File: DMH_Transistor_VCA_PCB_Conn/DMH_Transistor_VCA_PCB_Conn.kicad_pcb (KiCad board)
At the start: 2 copper layers, 48 x 175 mm, 0 parts

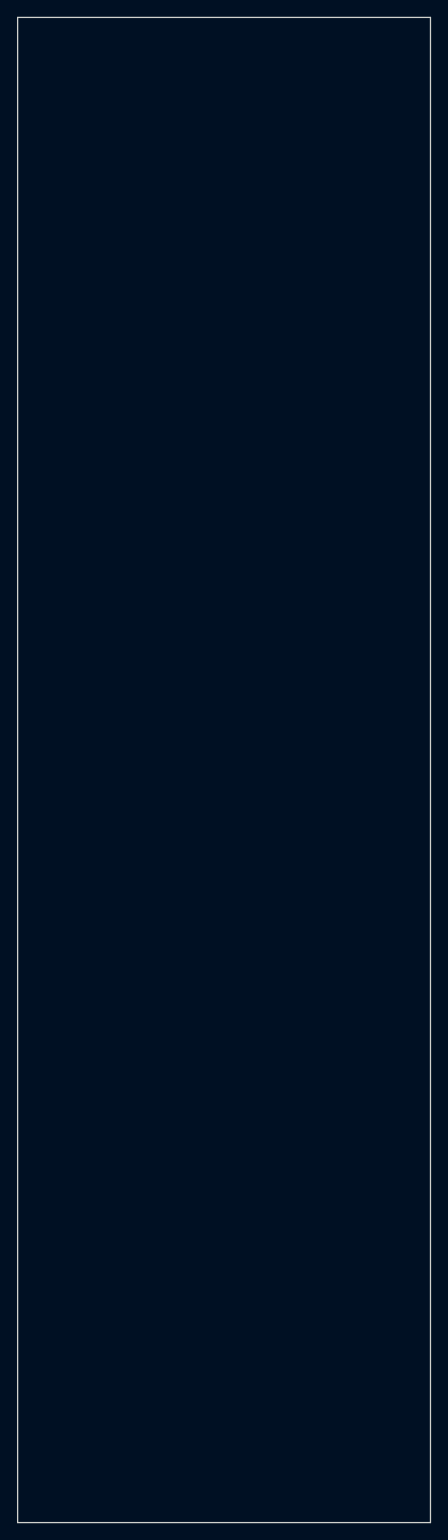
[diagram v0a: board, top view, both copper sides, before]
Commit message: Pots PCB in progress
Need to add CV input traces to the pin headers
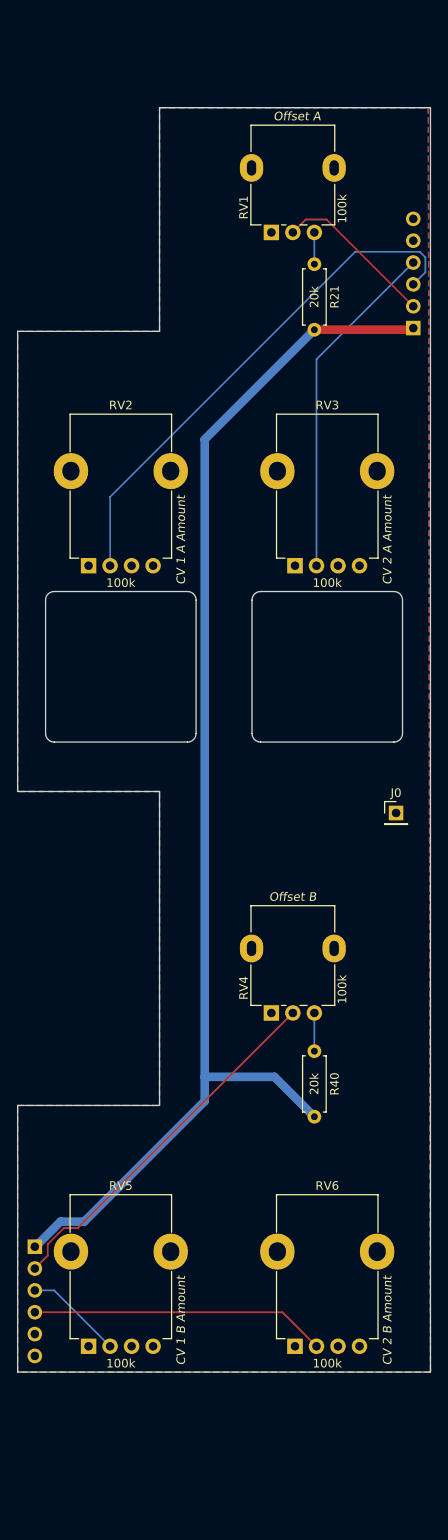
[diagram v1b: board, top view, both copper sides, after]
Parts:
- added J0: Conn_01x01, Connector_PinHeader_2.54mm:PinHeader_1x01_P2.54mm_Vertical, F.Cu at (95.0, 135.0)
- added J50: Conn_01x06, Connector_PinHeader_2.54mm:PinHeader_1x06_P2.54mm_Vertical, B.Cu at (97.0, 78.6)
- added J60: Conn_01x06, Connector_PinHeader_2.54mm:PinHeader_1x06_P2.54mm_Vertical, B.Cu at (53.0, 185.4)
- added R21: 20k, Resistor_THT:R_Axial_DIN0207_L6.3mm_D2.5mm_P7.62mm_Horizontal, F.Cu at (85.5, 71.2)
- added R40: 20k, Resistor_THT:R_Axial_DIN0207_L6.3mm_D2.5mm_P7.62mm_Horizontal, F.Cu at (85.5, 162.7)
- added RV1: 100k, SynthStuff:Potentiometer_Alpha_RD901F-40-00D_Single_Vertical, F.Cu at (80.5, 67.5)
- added RV2: 100k, SynthStuff:Potentiometer_TT_P110KH1, F.Cu at (60.5, 106.2)
- added RV3: 100k, SynthStuff:Potentiometer_TT_P110KH1, F.Cu at (84.5, 106.2)
- added RV4: 100k, SynthStuff:Potentiometer_Alpha_RD901F-40-00D_Single_Vertical, F.Cu at (80.5, 158.2)
- added RV5: 100k, SynthStuff:Potentiometer_TT_P110KH1, F.Cu at (60.5, 197.0)
- added RV6: 100k, SynthStuff:Potentiometer_TT_P110KH1, F.Cu at (84.5, 197.0)
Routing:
- net +12V: track 0.00 -> 148.0 mm
- net /Inputs and Outputs/CV 1 A Pot: track 0.00 -> 60.4 mm
- net /Inputs and Outputs/Offset B Pot: track 0.00 -> 43.1 mm
- net /Inputs and Outputs/CV 2 A Pot: track 0.00 -> 39.9 mm
- net /Inputs and Outputs/CV 2 B Pot: track 0.00 -> 34.4 mm
- net /Inputs and Outputs/Offset A Pot: track 0.00 -> 18.8 mm
- net /Inputs and Outputs/CV 1 B Pot: track 0.00 -> 11.4 mm
- net Net-(R40-Pad1): track 0.00 -> 4.44 mm
- net Net-(R21-Pad1): track 0.00 -> 3.69 mm
- added copper zone on B.Cu, net GND
- added copper zone on F.Cu, net GND
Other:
- board size 48 x 175 mm -> 48 x 147 mm

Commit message: Finished Pots PCB
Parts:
- J50, J60: value Conn_01x06 -> Conn_01x08; footprint Connector_PinHeader_2.54mm:PinHeader_1x06_P2.54mm_Vertical -> Connector_PinHeader_2.54mm:PinHeader_1x08_P2.54mm_Vertical
- moved J60 5.05 mm to (53.0, 180.4)
- moved J50 5.00 mm to (97.0, 83.6)
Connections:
- J50 pad 1: +12V -> /Inputs and Outputs/CV 1 A Jack
- J50 pad 2: /Inputs and Outputs/Offset A Pot -> /Inputs and Outputs/CV 2 A Jack
- J50 pad 3: /Inputs and Outputs/CV 1 A Pot -> +12V
- J50 pad 4: /Inputs and Outputs/CV 2 A Pot -> /Inputs and Outputs/Offset A Pot
- J50 pad 5: GND -> /Inputs and Outputs/CV 1 A Pot
- J50 pad 6: GND -> /Inputs and Outputs/CV 2 A Pot
- J60 pad 1: +12V -> /Inputs and Outputs/CV 1 B Jack
- J60 pad 2: /Inputs and Outputs/Offset B Pot -> /Inputs and Outputs/CV 2 B Jack
- J60 pad 3: /Inputs and Outputs/CV 1 B Pot -> +12V
- J60 pad 4: /Inputs and Outputs/CV 2 B Pot -> /Inputs and Outputs/Offset B Pot
- J60 pad 5: GND -> /Inputs and Outputs/CV 1 B Pot
- J60 pad 6: GND -> /Inputs and Outputs/CV 2 B Pot
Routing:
- net /Inputs and Outputs/CV 2 B Jack: track 0.00 -> 44.9 mm
- net /Inputs and Outputs/CV 1 A Jack: track 0.00 -> 42.1 mm
- net /Inputs and Outputs/CV 2 A Jack: track 0.00 -> 30.0 mm
- net /Inputs and Outputs/CV 1 B Jack: track 0.00 -> 27.8 mm

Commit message: Perfected pots (_conn) PCB
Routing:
- net /Inputs and Outputs/Offset B Pot: track 43.1 -> 45.4 mm
- net +12V: track 148.0 -> 146.8 mm
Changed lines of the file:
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@@
 			(pintype "passive")
 		)
-		(model "${KICAD8_3DMODEL_DIR}/Potentiometer_THT.3dshapes/Potentiometer_TT_P0915N.wrl"
+		(model "${KIPRJMOD}/Libraries/SynthStuff/3D_models/P110KH1_0F15BR10K.STEP"
 			(offset
-				(xyz 0 0 0)
+				(xyz 2.5 11 6)
 			)
 			(scale
@@
 			)
 			(rotate
-				(xyz 0 0 0)
+				(xyz 90 0 90)
 			)
 		)
@@
 			(pintype "passive")
 		)
-		(model "${KICAD8_3DMODEL_DIR}/Potentiometer_THT.3dshapes/Potentiometer_TT_P0915N.wrl"
+		(model "${KIPRJMOD}/Libraries/SynthStuff/3D_models/P110KH1_0F15BR10K.STEP"
 			(offset
-				(xyz 0 0 0)
+				(xyz 2.5 11 6)
 			)
 			(scale
@@
 			)
 			(rotate
-				(xyz 0 0 0)
+				(xyz 90 0 90)
 			)
 		)
 	)
 	(footprint "Connector_PinHeader_2.54mm:PinHeader_1x01_P2.54mm_Vertical"
-		(locked yes)
 		(layer "F.Cu")
 		(at 95 135)
@@
 		(sheetname "Inputs and Outputs")
 		(sheetfile "Inputs_and_Outputs.kicad_sch")
-		(attr through_hole)
+		(attr through_hole exclude_from_bom dnp)
 		(fp_line
 			(start -1.33 -1.33)
@@
 			(pintype "passive")
 		)
-		(model "${KICAD8_3DMODEL_DIR}/Potentiometer_THT.3dshapes/Potentiometer_TT_P0915N.wrl"
+		(model "${KIPRJMOD}/Libraries/SynthStuff/3D_models/P110KH1_0F15BR10K.STEP"
 			(offset
-				(xyz 0 0 0)
+				(xyz 2.5 11 6)
 			)
 			(scale
@@
 			)
 			(rotate
-				(xyz 0 0 0)
+				(xyz 90 0 90)
 			)
 		)
@@
 			(pintype "passive")
 		)
-		(model "${KICAD8_3DMODEL_DIR}/Potentiometer_THT.3dshapes/Potentiometer_TT_P0915N.wrl"
+		(model "${KIPRJMOD}/Libraries/SynthStuff/3D_models/P110KH1_0F15BR10K.STEP"
 			(offset
-				(xyz 0 0 0)
+				(xyz 2.5 11 6)
 			)
 			(scale
@@
 			)
 			(rotate
-				(xyz 0 0 0)
+				(xyz 90 0 90)
 			)
 		)
@@
 	)
 	(segment
-		(start 51.6 181.775)
-		(end 51.6 193.541346)
+		(start 61.5 194.25)
+		(end 64.25 197)
 		(width 0.2)
 		(layer "F.Cu")
@@
 	)
 	(segment
-		(start 51.6 193.541346)
-		(end 52.523654 194.465)
+		(start 52.308654 194.25)
+		(end 61.5 194.25)
 		(width 0.2)
 		(layer "F.Cu")
@@
 	)
 	(segment
-		(start 52.523654 194.465)
-		(end 61.715 194.465)
+		(start 51.6 181.775)
+		(end 51.6 193.541346)
 		(width 0.2)
 		(layer "F.Cu")
@@
 	)
 	(segment
-		(start 61.715 194.465)
-		(end 64.25 197)
+		(start 51.6 193.541346)
+		(end 52.308654 194.25)
 		(width 0.2)
 		(layer "F.Cu")
@@
 	)
 	(segment
-		(start 51.6 184.315)
-		(end 51.6 186.1)
+		(start 53 182.915)
+		(end 51.6 184.315)
 		(width 0.2)
 		(layer "B.Cu")
@@
 	)
 	(segment
-		(start 52.25 186.75)
-		(end 54.597309 186.75)
+		(start 85.5 194.25)
+		(end 88.25 197)
 		(width 0.2)
 		(layer "B.Cu")
@@
 	)
 	(segment
-		(start 85.5 194.25)
-		(end 88.25 197)
+		(start 61.75 194.25)
+		(end 85.5 194.25)
 		(width 0.2)
 		(layer "B.Cu")
@@
 	)
 	(segment
-		(start 62.097309 194.25)
-		(end 85.5 194.25)
+		(start 51.6 184.315)
+		(end 51.6 186.1)
 		(width 0.2)
 		(layer "B.Cu")
@@
 	)
 	(segment
-		(start 53 182.915)
-		(end 51.6 184.315)
+		(start 52.25 186.75)
+		(end 54.25 186.75)
 		(width 0.2)
 		(layer "B.Cu")
@@
 	)
 	(segment
-		(start 54.597309 186.75)
-		(end 62.097309 194.25)
+		(start 54.25 186.75)
+		(end 61.75 194.25)
 		(width 0.2)
 		(layer "B.Cu")
@@
 	)
 	(segment
-		(start 54.5 186.465)
-		(end 53 187.965)
+		(start 83 161.75)
+		(end 61.5 183.25)
 		(width 0.2)
 		(layer "F.Cu")
@@
 	)
 	(segment
-		(start 54.5 185.15)
+		(start 54.5 184.75)
 		(end 54.5 186.465)
 		(width 0.2)
@@
 	)
 	(segment
-		(start 58 183.25)
-		(end 56.4 183.25)
+		(start 83 158.25)
+		(end 83 161.75)
 		(width 0.2)
 		(layer "F.Cu")
@@
 	)
 	(segment
-		(start 83 158.25)
-		(end 58 183.25)
+		(start 56 183.25)
+		(end 54.5 184.75)
+		(width 0.2)
+		(layer "F.Cu")
+		(net 10)
+	)
+	(segment
+		(start 61.5 183.25)
+		(end 56 183.25)
 		(width 0.2)
 		(layer "F.Cu")
@@
 	)
 	(segment
-		(start 56.4 183.25)
-		(end 54.5 185.15)
+		(start 54.5 186.465)
+		(end 53 187.965)
 		(width 0.2)
 		(layer "F.Cu")
@@
 	)
 	(segment
-		(start 80.865 165.675)
-		(end 85.5 170.31)
-		(width 1)
-		(layer "B.Cu")
-		(net 12)
-	)
-	(segment
 		(start 58.75 182.5)
 		(end 56 182.5)
@@
 	)
 	(segment
-		(start 72.75 165.675)
-		(end 72.75 168.5)
+		(start 72.75 168.5)
+		(end 83.69 168.5)
 		(width 1)
 		(layer "B.Cu")
@@
 	)
 	(segment
-		(start 96.81 78.81)
-		(end 97 78.62)
+		(start 83.69 168.5)
+		(end 85.5 170.31)
 		(width 1)
 		(layer "B.Cu")
@@
 	(segment
 		(start 72.75 165.675)
-		(end 80.865 165.675)
+		(end 72.75 168.5)
+		(width 1)
+		(layer "B.Cu")
+		(net 12)
+	)
+	(segment
+		(start 96.81 78.81)
+		(end 97 78.62)
 		(width 1)
 		(layer "B.Cu")

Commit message: Generated Gerbers
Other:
- board text added: "Mk1.0 - March 2025"
- board text removed: "Mk1.0 - Month Year"
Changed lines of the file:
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@@
 			(plot_on_all_layers_selection 0x00000000_00000000_00000000_00000000)
 			(disableapertmacros no)
-			(usegerberextensions no)
+			(usegerberextensions yes)
 			(usegerberattributes yes)
 			(usegerberadvancedattributes yes)
@@
 			(sketchdnponfab yes)
 			(crossoutdnponfab yes)
-			(subtractmaskfromsilk no)
+			(subtractmaskfromsilk yes)
 			(outputformat 1)
 			(mirror no)
-			(drillshape 1)
+			(drillshape 0)
 			(scaleselection 1)
-			(outputdirectory "")
+			(outputdirectory "Gerbers/")
 		)
 	)
@@
 		(layer "User.9")
 	)
-	(gr_text "Mk1.0 - Month Year"
+	(gr_text "Mk1.0 - March 2025"
 		(at 97.75 167 90)
 		(layer "B.SilkS")
